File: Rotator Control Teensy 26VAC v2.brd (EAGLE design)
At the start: 88.9 x 81.3 mm, 63 parts, among them K1 G5LE, K2 G5LE, K3 G5LE, Q1 BSS123, Q2 BSS123, Q3 BSS123, U2 MAX6959BAEE+, X1 Rotor, X2 26VAC

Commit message: Add pullups on I2C lines Add holes for 7 segment LED with 0.4 in lead spacing
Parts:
- added R2, R3: 2.2K, rcl:R0805
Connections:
- net +5V: now also R2.2, R3.2
- net SCL0: now also R2.1
- net SDA0: now also R3.1
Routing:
- net SCL0: track 41.2 -> 47.7 mm, vias 2 -> 4
- net SDA0: track 46.1 -> 51.2 mm, vias 2 -> 3
- net DIG3: track 41.3 -> 44.0 mm, vias 2 -> 3
- net SEG6: track 26.7 -> 29.2 mm, vias 1 -> 2
- net SEG5: track 30.8 -> 33.3 mm, vias 1 -> 2
- net SEG4: track 32.3 -> 34.9 mm, vias 0 -> 1
- net DIG2: track 40.2 -> 42.8 mm, vias 0 -> 1
- net +5V: track 157.2 -> 159.7 mm
- net SEG9: track 61.1 -> 62.9 mm, vias 1 -> 2
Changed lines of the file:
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@@
 <attribute name="VALUE" x="19.05" y="5.715" size="1.27" layer="27" rot="R270"/>
+</element>
+<element name="R2" library="rcl" library_urn="urn:adsk.eagle:library:334" package="R0805" package3d_urn="urn:adsk.eagle:package:23553/2" value="2.2K" x="36.83" y="69.85" smashed="yes">
+<attribute name="NAME" x="38.989" y="69.342" size="1.27" layer="25"/>
+<attribute name="POPULARITY" value="85" x="36.83" y="69.85" size="1.778" layer="27" display="off"/>
+<attribute name="SPICEPREFIX" value="R" x="36.83" y="69.85" size="1.778" layer="27" display="off"/>
+<attribute name="VALUE" x="36.195" y="67.31" size="1.27" layer="27"/>
+</element>
+<element name="R3" library="rcl" library_urn="urn:adsk.eagle:library:334" package="R0805" package3d_urn="urn:adsk.eagle:package:23553/2" value="2.2K" x="27.94" y="69.85" smashed="yes">
+<attribute name="NAME" x="23.495" y="69.342" size="1.27" layer="25"/>
+<attribute name="POPULARITY" value="85" x="27.94" y="69.85" size="1.778" layer="27" display="off"/>
+<attribute name="SPICEPREFIX" value="R" x="27.94" y="69.85" size="1.778" layer="27" display="off"/>
+<attribute name="VALUE" x="27.305" y="67.31" size="1.27" layer="27"/>
 </element>
 </elements>
@@
 <wire x1="29.525" y1="24.511" x2="35.687" y2="24.511" width="0.8128" layer="1"/>
 <wire x1="24.13" y1="64.77" x2="24.13" y2="68.58" width="0.508" layer="1"/>
-<wire x1="24.13" y1="68.58" x2="40.64" y2="68.58" width="0.508" layer="1"/>
+<wire x1="24.13" y1="68.58" x2="28.89" y2="68.58" width="0.508" layer="1"/>
 <via x="40.64" y="68.58" extent="1-16" drill="0.35"/>
+<wire x1="37.78" y1="68.58" x2="40.64" y2="68.58" width="0.508" layer="1"/>
 <wire x1="40.64" y1="68.58" x2="45.72" y2="68.58" width="0.508" layer="16"/>
 <via x="45.72" y="68.58" extent="1-16" drill="0.35"/>
@@
 <contactref element="R5" pad="2"/>
 <wire x1="17.78" y1="4.13" x2="21.59" y2="4.13" width="0.508" layer="1"/>
+<contactref element="R2" pad="2"/>
+<contactref element="R3" pad="2"/>
+<wire x1="28.89" y1="69.85" x2="28.89" y2="68.58" width="0.4064" layer="1"/>
+<wire x1="37.78" y1="69.85" x2="37.78" y2="68.58" width="0.4064" layer="1"/>
+<wire x1="28.89" y1="68.58" x2="37.78" y2="68.58" width="0.508" layer="1"/>
 </signal>
 <signal name="N$12">
@@
 <wire x1="66.04" y1="69.85" x2="64.77" y2="71.12" width="0.4064" layer="1"/>
 <wire x1="64.77" y1="71.12" x2="45.72" y2="71.12" width="0.4064" layer="1"/>
+<via x="66.04" y="58.42" extent="1-16" drill="0.75" diameter="1.27"/>
+<wire x1="66.04" y1="60.96" x2="66.04" y2="58.42" width="0.4064" layer="1"/>
 </signal>
 <signal name="DIG3">
@@
 <contactref element="LED5" pad="10"/>
 <contactref element="LED5" pad="6"/>
-<wire x1="43.857725" y1="59.4912" x2="63.3012" y2="59.4912" width="0.4064" layer="1"/>
-<wire x1="63.3012" y1="59.4912" x2="63.5" y2="59.69" width="0.4064" layer="1"/>
-<wire x1="63.5" y1="59.69" x2="63.5" y2="60.96" width="0.4064" layer="1"/>
+<wire x1="43.857725" y1="59.4912" x2="63.5" y2="59.4912" width="0.4064" layer="1"/>
 <wire x1="71.12" y1="68.58" x2="71.12" y2="66.04" width="0.4064" layer="16"/>
 <via x="71.12" y="66.04" extent="1-16" drill="0.35"/>
@@
 <wire x1="64.77" y1="63.5" x2="63.5" y2="62.23" width="0.4064" layer="16"/>
 <wire x1="63.5" y1="62.23" x2="63.5" y2="60.96" width="0.4064" layer="16"/>
+<via x="63.5" y="58.42" extent="1-16" drill="0.75" diameter="1.27"/>
+<wire x1="63.5" y1="60.96" x2="63.5" y2="59.4912" width="0.4064" layer="1"/>
+<wire x1="63.5" y1="58.42" x2="63.5" y2="60.96" width="0.4064" layer="1"/>
 </signal>
 <signal name="SEG4">
@@
 <contactref element="LED5" pad="1"/>
 <wire x1="76.2" y1="60.96" x2="76.2" y2="62.23" width="0.4064" layer="1"/>
+<via x="76.2" y="58.42" extent="1-16" drill="0.75" diameter="1.27" shape="square"/>
+<wire x1="76.2" y1="60.96" x2="76.2" y2="58.42" width="0.4064" layer="1"/>
 </signal>
 <signal name="SEG5">
@@
 <contactref element="LED5" pad="2"/>
 <wire x1="73.66" y1="60.96" x2="73.66" y2="63.5" width="0.4064" layer="16"/>
+<via x="73.66" y="58.42" extent="1-16" drill="0.75" diameter="1.27"/>
+<wire x1="73.66" y1="60.96" x2="73.66" y2="58.42" width="0.4064" layer="1"/>
 </signal>
 <signal name="SEG6">
@@
 <contactref element="LED5" pad="4"/>
 <wire x1="68.58" y1="60.96" x2="68.58" y2="64.77" width="0.4064" layer="16"/>
+<via x="68.58" y="58.42" extent="1-16" drill="0.75" diameter="1.27"/>
+<wire x1="68.58" y1="60.96" x2="68.58" y2="58.42" width="0.4064" layer="1"/>
 </signal>
 <signal name="SEG7">
@@
 </signal>
 <signal name="SEG9">
-<wire x1="43.439315625" y1="73.919315625" x2="43.75450625" y2="73.9394" width="0.4064" layer="1"/>
-<wire x1="43.75450625" y1="73.9394" x2="73.66" y2="73.9394" width="0.4064" layer="1"/>
+<wire x1="44.7294" y1="73.9394" x2="73.66" y2="73.9394" width="0.4064" layer="1"/>
 <via x="71.12" y="64.77" extent="1-16" drill="0.35"/>
 <wire x1="71.12" y1="64.77" x2="77.47" y2="64.77" width="0.4064" layer="1"/>
@@
 <wire x1="77.47" y1="64.77" x2="77.47" y2="70.1294" width="0.4064" layer="1"/>
 <wire x1="41.4975" y1="65.7225" x2="41.91" y2="66.135" width="0.4064" layer="1"/>
-<wire x1="41.91" y1="66.135" x2="41.91" y2="72.39" width="0.4064" layer="1"/>
-<wire x1="41.91" y1="72.39" x2="43.439315625" y2="73.919315625" width="0.4064" layer="1"/>
+<wire x1="41.91" y1="66.135" x2="41.91" y2="71.12" width="0.4064" layer="1"/>
+<wire x1="41.91" y1="71.12" x2="44.7294" y2="73.9394" width="0.4064" layer="1"/>
 <contactref element="U2" pad="3"/>
 <wire x1="40.545" y1="65.7225" x2="41.4975" y2="65.7225" width="0.4064" layer="1"/>
 <contactref element="LED5" pad="3"/>
 <wire x1="71.12" y1="60.96" x2="71.12" y2="64.77" width="0.4064" layer="16"/>
+<via x="71.12" y="58.42" extent="1-16" drill="0.75" diameter="1.27"/>
+<wire x1="71.12" y1="60.96" x2="71.12" y2="58.42" width="0.4064" layer="1"/>
 </signal>
 <signal name="N$13">
@@
 <contactref element="U$1" pad="19/A5/SCL"/>
 <wire x1="38.1" y1="66.04" x2="38.4175" y2="66.3575" width="0.4064" layer="1"/>
-<wire x1="22.86" y1="66.04" x2="19.05" y2="66.04" width="0.4064" layer="1"/>
-<wire x1="20.32" y1="46.99" x2="19.05" y2="48.26" width="0.4064" layer="1"/>
-<wire x1="19.05" y1="66.04" x2="19.05" y2="48.26" width="0.4064" layer="1"/>
 <contactref element="U2" pad="2"/>
 <wire x1="40.545" y1="66.3575" x2="38.4175" y2="66.3575" width="0.4064" layer="1"/>
@@
 <wire x1="22.86" y1="66.04" x2="25.4" y2="66.04" width="0.4064" layer="16"/>
 <via x="25.4" y="66.04" extent="1-16" drill="0.35"/>
-<wire x1="25.4" y1="66.04" x2="38.1" y2="66.04" width="0.4064" layer="1"/>
+<wire x1="25.4" y1="66.04" x2="34.29" y2="66.04" width="0.4064" layer="1"/>
+<contactref element="R2" pad="1"/>
+<wire x1="34.29" y1="66.04" x2="38.1" y2="66.04" width="0.4064" layer="1"/>
+<wire x1="22.86" y1="66.04" x2="19.05" y2="66.04" width="0.4064" layer="1"/>
+<wire x1="19.05" y1="66.04" x2="17.78" y2="64.77" width="0.4064" layer="1"/>
+<wire x1="17.78" y1="64.77" x2="17.78" y2="49.53" width="0.4064" layer="1"/>
+<wire x1="17.78" y1="49.53" x2="20.32" y2="46.99" width="0.4064" layer="1"/>
+<wire x1="35.88" y1="69.85" x2="34.29" y2="69.85" width="0.4064" layer="1"/>
+<via x="34.29" y="69.85" extent="1-16" drill="0.35"/>
+<wire x1="34.29" y1="69.85" x2="34.29" y2="66.04" width="0.4064" layer="16"/>
+<via x="34.29" y="66.04" extent="1-16" drill="0.35"/>
 </signal>
 <signal name="SDA0">
 <contactref element="U$1" pad="18/A4/SDA"/>
-<wire x1="22.86" y1="67.31" x2="19.05" y2="67.31" width="0.4064" layer="1"/>
-<wire x1="19.05" y1="67.31" x2="17.78" y2="66.04" width="0.4064" layer="1"/>
-<wire x1="17.78" y1="66.04" x2="17.78" y2="46.99" width="0.4064" layer="1"/>
-<wire x1="20.32" y1="44.45" x2="17.78" y2="46.99" width="0.4064" layer="1"/>
 <contactref element="U2" pad="1"/>
 <wire x1="40.545" y1="66.9925" x2="38.005" y2="66.9925" width="0.4064" layer="1"/>
@@
 <via x="25.4" y="67.31" extent="1-16" drill="0.35"/>
 <wire x1="22.86" y1="67.31" x2="25.4" y2="67.31" width="0.4064" layer="16"/>
+<contactref element="R3" pad="1"/>
+<wire x1="22.86" y1="67.31" x2="19.05" y2="67.31" width="0.4064" layer="1"/>
+<wire x1="19.05" y1="67.31" x2="16.51" y2="64.77" width="0.4064" layer="1"/>
+<wire x1="16.51" y1="64.77" x2="16.51" y2="48.26" width="0.4064" layer="1"/>
+<wire x1="16.51" y1="48.26" x2="20.32" y2="44.45" width="0.4064" layer="1"/>
+<wire x1="26.99" y1="69.85" x2="25.4" y2="69.85" width="0.4064" layer="1"/>
+<via x="25.4" y="69.85" extent="1-16" drill="0.35"/>
+<wire x1="25.4" y1="69.85" x2="25.4" y2="67.31" width="0.4064" layer="16"/>
 </signal>
 <signal name="N$15">

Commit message: move rotator pot pullups from 5V to regulated 3.3V.  5V varied from USB to USB and changed when relays activated...which changed the azimuth calibration
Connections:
- net +3V3: now also R5.2, R6.2
- net +5V: no longer R5.2, R6.2
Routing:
- net +3V3: track 31.8 -> 42.7 mm
- net +5V: track 159.7 -> 149.8 mm, vias 4 -> 2
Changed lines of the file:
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@@
 </element>
 <element name="R3" library="rcl" library_urn="urn:adsk.eagle:library:334" package="R0805" package3d_urn="urn:adsk.eagle:package:23553/2" value="2.2K" x="27.94" y="69.85" smashed="yes">
-<attribute name="NAME" x="23.495" y="69.342" size="1.27" layer="25"/>
+<attribute name="NAME" x="30.099" y="69.342" size="1.27" layer="25"/>
 <attribute name="POPULARITY" value="85" x="27.94" y="69.85" size="1.778" layer="27" display="off"/>
 <attribute name="SPICEPREFIX" value="R" x="27.94" y="69.85" size="1.778" layer="27" display="off"/>
@@
 <contactref element="C3" pad="1"/>
 <wire x1="78.74" y1="24.13" x2="75.06" y2="24.13" width="1.27" layer="16"/>
-<wire x1="47.879" y1="24.511" x2="51.054" y2="24.511" width="1.778" layer="1"/>
-<wire x1="51.054" y1="24.511" x2="51.054" y2="24.13" width="1.778" layer="1"/>
-<wire x1="78.74" y1="24.13" x2="51.054" y2="24.13" width="1.778" layer="1"/>
+<wire x1="47.879" y1="24.511" x2="49.784" y2="24.511" width="1.778" layer="1"/>
+<wire x1="49.784" y1="24.511" x2="49.784" y2="24.13" width="1.778" layer="1"/>
+<wire x1="78.74" y1="24.13" x2="49.784" y2="24.13" width="1.778" layer="1"/>
 </signal>
 <signal name="LEFT">
@@
 <wire x1="17.315" y1="9.21" x2="15.56" y2="9.21" width="0.508" layer="1"/>
 <wire x1="15.56" y1="9.21" x2="15.24" y2="8.89" width="0.508" layer="1"/>
+<contactref element="R6" pad="2"/>
+<contactref element="R5" pad="2"/>
+<wire x1="17.78" y1="4.13" x2="19.558" y2="4.13" width="0.508" layer="1"/>
+<wire x1="19.558" y1="4.13" x2="21.59" y2="4.13" width="0.508" layer="1"/>
+<wire x1="17.315" y1="9.21" x2="17.315" y2="8.085" width="0.508" layer="1"/>
+<wire x1="17.315" y1="8.085" x2="17.78" y2="7.62" width="0.508" layer="1"/>
+<wire x1="17.78" y1="7.62" x2="19.558" y2="7.62" width="0.508" layer="1"/>
+<wire x1="19.558" y1="7.62" x2="19.558" y2="4.13" width="0.508" layer="1"/>
 </signal>
 <signal name="N$4">
@@
 <wire x1="45.72" y1="68.58" x2="48.13" y2="68.58" width="0.508" layer="1"/>
 <wire x1="24.13" y1="24.511" x2="24.13" y2="6.731" width="0.8128" layer="1"/>
-<contactref element="R6" pad="2"/>
-<wire x1="21.59" y1="4.13" x2="22.86" y2="4.13" width="0.508" layer="1"/>
-<wire x1="23.18" y1="3.81" x2="22.86" y2="4.13" width="0.508" layer="1"/>
-<via x="24.13" y="3.81" extent="1-16" drill="0.35"/>
-<wire x1="23.18" y1="3.81" x2="24.13" y2="3.81" width="0.508" layer="1"/>
-<wire x1="24.13" y1="3.81" x2="25.4" y2="5.08" width="0.508" layer="16"/>
-<via x="25.4" y="5.08" extent="1-16" drill="0.35"/>
-<wire x1="25.4" y1="5.08" x2="25.4" y2="6.731" width="0.508" layer="1"/>
-<contactref element="R5" pad="2"/>
-<wire x1="17.78" y1="4.13" x2="21.59" y2="4.13" width="0.508" layer="1"/>
 <contactref element="R2" pad="2"/>
 <contactref element="R3" pad="2"/>

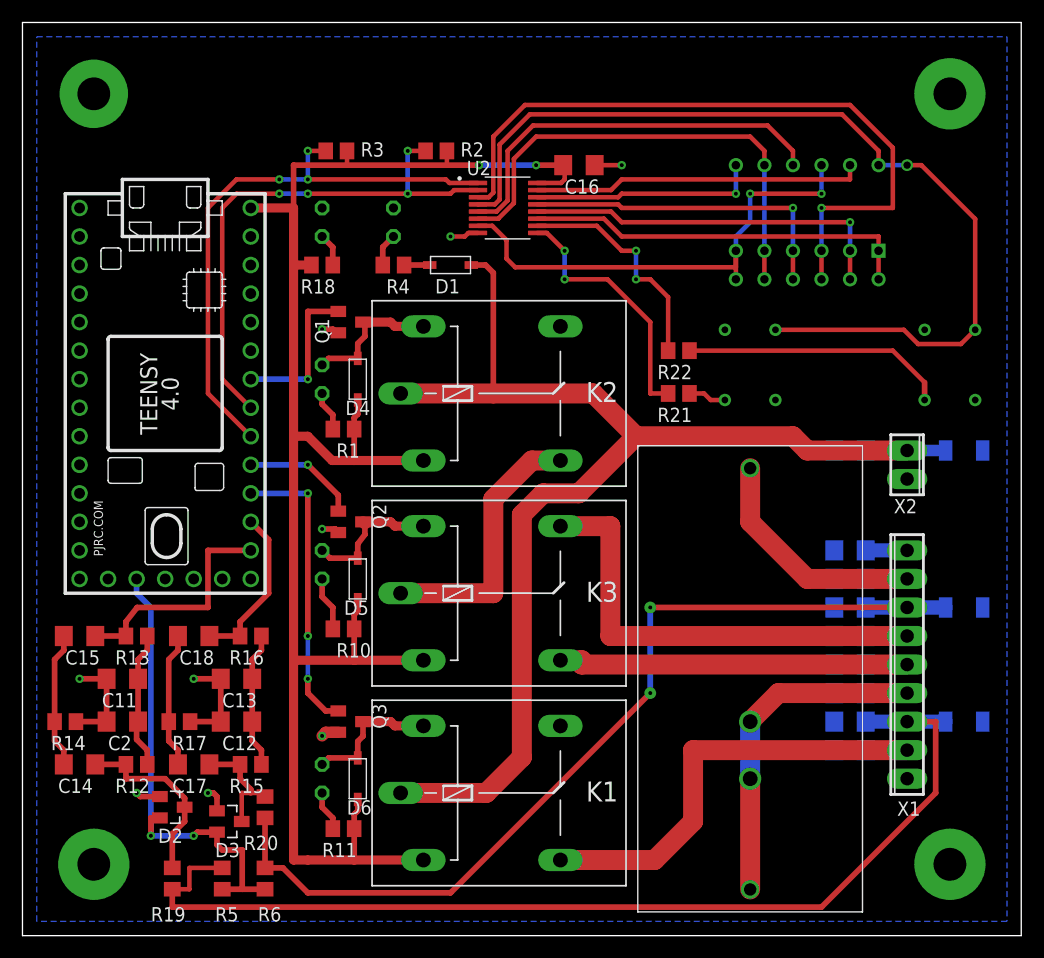
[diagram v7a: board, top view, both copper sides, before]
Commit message: Convert to MAX7221 LED driver Connect MAX7221 to SPI port Convert buttons to direct read with internal pullups
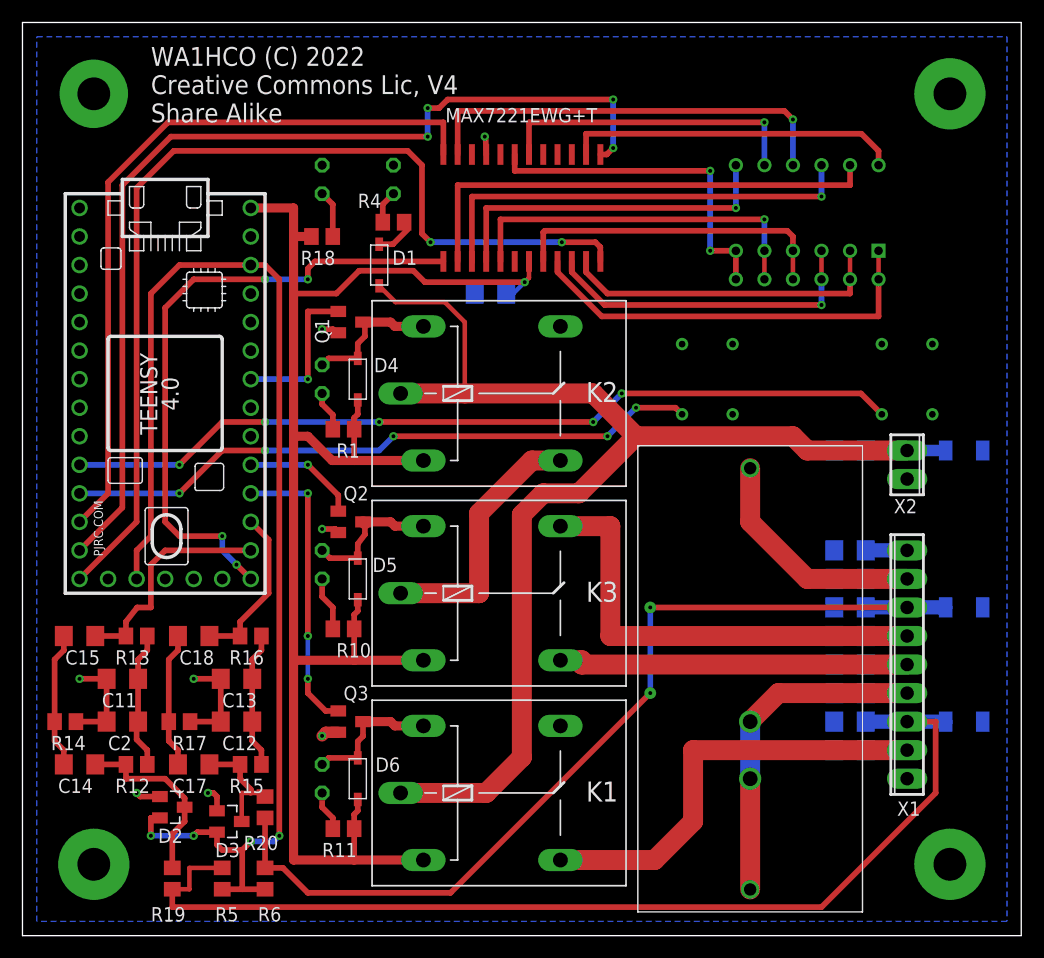
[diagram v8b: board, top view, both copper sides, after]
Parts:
- removed R2, R3: 2.2K, rcl:R0805
- removed R21, R22: 39K, rcl:R0805
- removed U$2, U$3: SWITCH_AEXIT_6X6X9.5, my-library:PUSHBUTTON_6X6
- removed U2: MAX6959BAEE+, MAX6959BAEE_:SOP63P602X175-16N
- added CCW, CW: SWITCH_AEXIT_6X6X9.5, my-library:PUSHBUTTON_6X6
- added U1: MAX7221EWG+T, MAX7219:21-0042_W24+1_MXM
- moved C16 13.9 mm to (41.7, 57.1), flipped to the bottom
- moved D1 6.35 mm to (31.8, 59.7), turned to 270 degrees
- moved LED4 3.81 mm to (33.0, 67.3)
- moved LED6 3.81 mm to (26.7, 67.3)
- moved R4 3.81 mm to (33.0, 63.5)
- moved R18 2.54 mm to (26.7, 62.2)
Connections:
- removed net +3V3: D2.2, D3.2, R5.2, R6.2, U$1.3V3_LN
- removed net N$15: R21.1, U2.9
- removed net N$16: R22.1, U2.10
- removed net N$19: R21.2, U$3.P$2
- removed net N$20: R22.2, U$2.P$2
- removed net SCL0: R2.1, U$1.19/A5/SCL, U2.2
- removed net SDA0: R3.1, U$1.18/A4/SDA, U2.1
- removed net SEG4: LED5.1, U2.11
- removed net SEG5: LED5.2, U2.12
- removed net SEG6: LED5.4, U2.13
- removed net SEG7: LED5.7, U2.14
- removed net SEG8: LED5.11, U2.15
- removed net SEG9: LED5.3, U2.3
- new net 3V3: D2.2, D3.2, R5.2, R6.2, U$1.3V3_LN, U$1.3V3_LO
- new net CCW*: CCW.P$2, U$1.8
- new net CS: U$1.10/CS, U1.12
- new net CW*: CW.P$2, U$1.9/CS
- new net MISO: U$1.12/MISO, U1.24
- new net MOSI: U$1.11/MOSI, U1.1
- new net SCK: U$1.13/SCK, U1.13
- new net SEGA: LED5.11, U1.14
- new net SEGB: LED5.7, U1.16
- new net SEGC: LED5.4, U1.20
- new net SEGD: LED5.2, U1.23
- new net SEGDP: LED5.3, U1.22
- new net SEGE: LED5.1, U1.21
- new net SEGF: LED5.10, U1.15
- new net SEGG: LED5.5, U1.17
- net +5V: now also U1.19; no longer R2.2, R3.2, U2.16
- net DIG0: now also U1.2; no longer U$2.P$1, U$3.P$1, U2.4
- net DIG1: now also U1.11; no longer U2.5
- net DIG2: now also U1.6; no longer LED5.5, U2.6
- net DIG3: now also U1.7; no longer LED5.10, U2.7
- net GND: now also CCW.P$1, CW.P$1, U1.9; no longer U$1.GND3, U2.8
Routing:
- net 3V3: track 0.00 -> 111.6 mm, vias 0 -> 4
- net MOSI: track 0.00 -> 88.1 mm, vias 0 -> 4
- net MISO: track 0.00 -> 87.9 mm, vias 0 -> 2
- net CCW*: track 0.00 -> 74.8 mm, vias 0 -> 5
- net CS: track 0.00 -> 66.2 mm
- net SEG9: track 62.9 -> 0.00 mm, vias 2 -> 0
- net CW*: track 0.00 -> 57.0 mm, vias 0 -> 5
- net SCK: track 0.00 -> 56.6 mm, vias 0 -> 4
- net DIG0: track 83.7 -> 29.8 mm, vias 1 -> 0
- net SDA0: track 51.2 -> 0.00 mm, vias 3 -> 0
- net SCL0: track 47.7 -> 0.00 mm, vias 4 -> 0
- net SEGA: track 0.00 -> 43.5 mm
- net +3V3: track 42.7 -> 0.00 mm, vias 2 -> 0
- net SEGF: track 0.00 -> 39.7 mm, vias 0 -> 1
- net SEGE: track 0.00 -> 37.0 mm, vias 0 -> 1
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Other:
- board text added: "CCW"
- board text added: "CW"
